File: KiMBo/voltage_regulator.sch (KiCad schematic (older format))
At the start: 13 parts

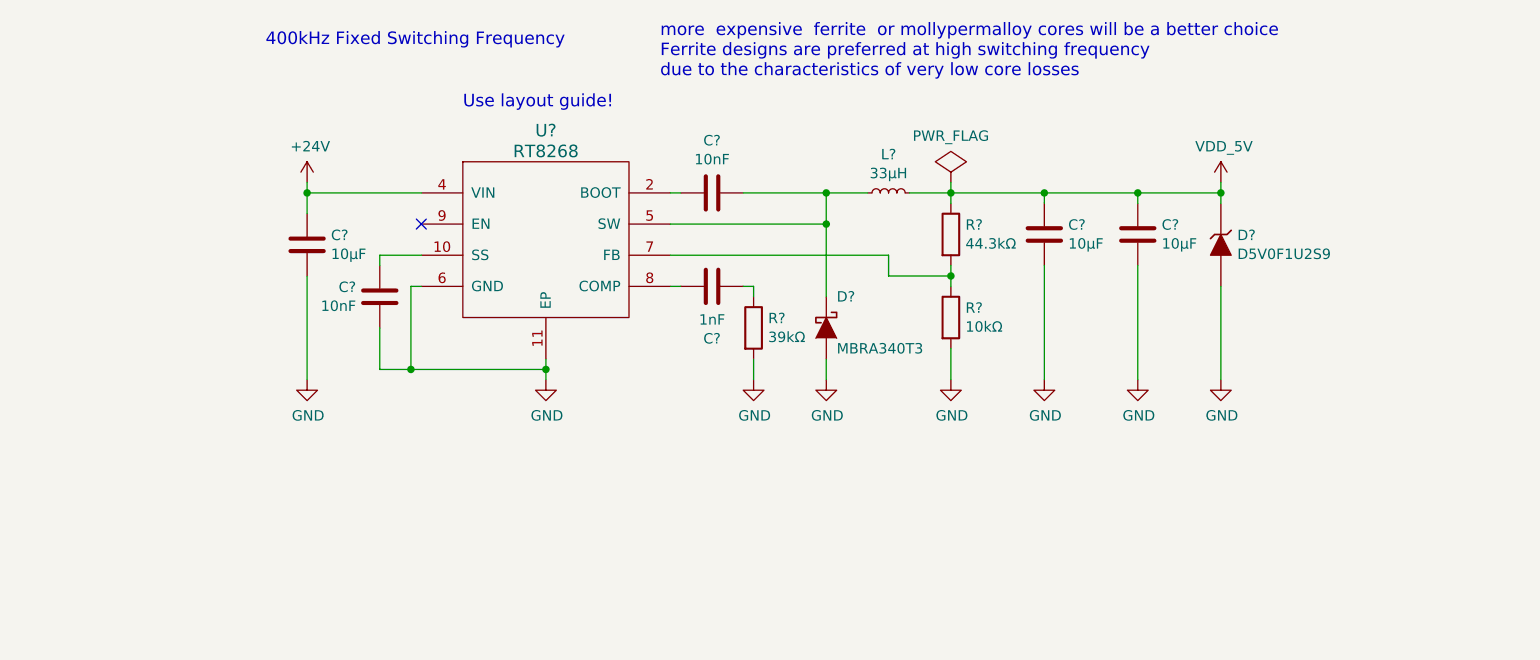
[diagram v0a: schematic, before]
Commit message: Move EN and SS lines, update 5V regulator passive values
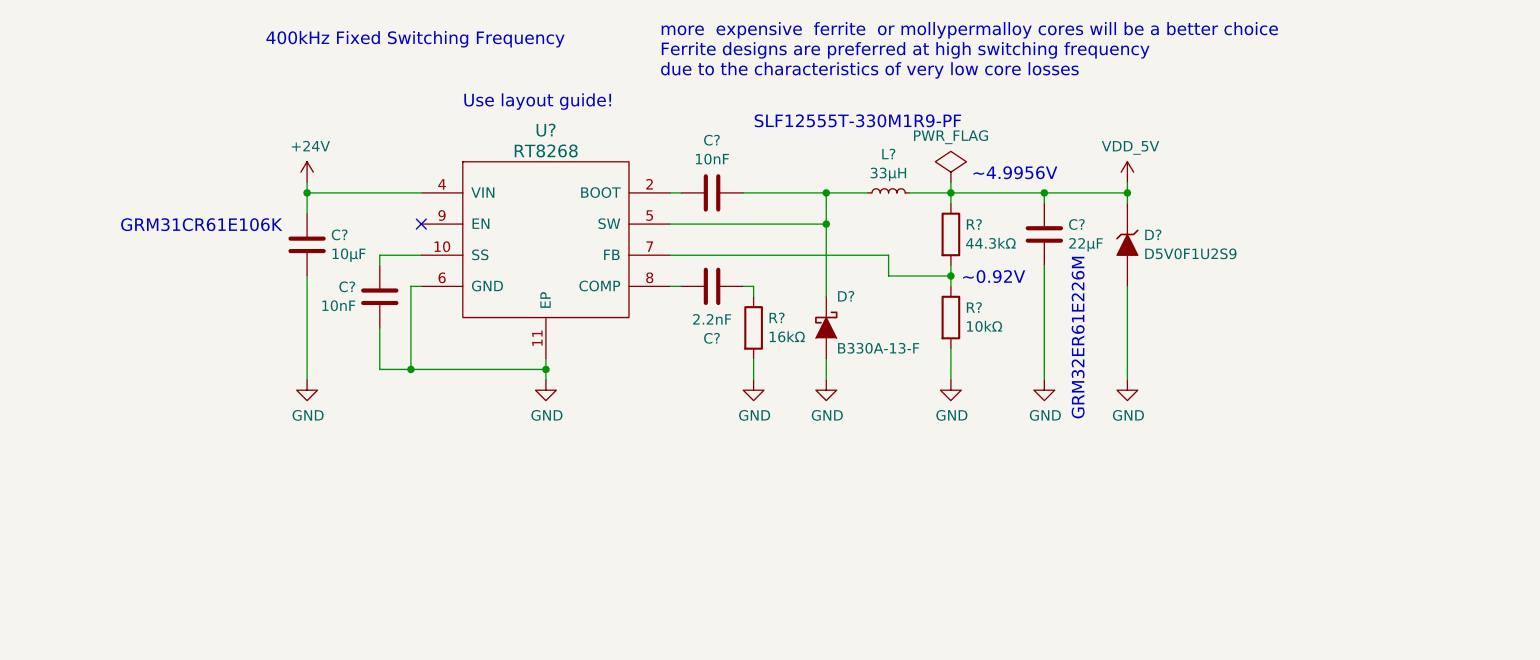
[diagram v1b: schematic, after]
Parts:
- removed C?: 10μF, symbol C
- C?: value 1nF -> 2.2nF
- C?: value 10μF -> 22μF
- D?: value MBRA340T3 -> B330A-13-F
- R?: value 39kΩ -> 16kΩ
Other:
- note added: "GRM31CR61E106K"
- note added: "GRM32ER61E226M"
- note added: "SLF12555T-330M1R9-PF"
- note added: "~~0.92V"
- note added: "~~4.9956V"
- moved on the sheet: D?
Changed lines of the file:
@@
 $EndDescr
 $Comp
-L PWR_FLAG #FLG053
+L PWR_FLAG #FLG074
 U 1 1 578901B0
 P 9250 4200
-F 0 "#FLG053" H 9250 4295 50  0001 C CNN
+F 0 "#FLG074" H 9250 4295 50  0001 C CNN
 F 1 "PWR_FLAG" H 9250 4424 50  0000 C CNN
 F 2 "" H 9250 4200 50  0000 C CNN
@@
 $EndComp
 $Comp
-L VDD_5V #PWR?
+L VDD_5V #PWR075
 U 1 1 59E9FFBE
-P 10550 4200
-F 0 "#PWR?" H 10550 4050 50  0001 C CNN
-F 1 "VDD_5V" H 10565 4373 50  0000 C CNN
-F 2 "" H 10550 4200 50  0000 C CNN
-F 3 "" H 10550 4200 50  0000 C CNN
-	1    10550 4200
+P 10100 4200
+F 0 "#PWR075" H 10100 4050 50  0001 C CNN
+F 1 "VDD_5V" H 10115 4373 50  0000 C CNN
+F 2 "" H 10100 4200 50  0000 C CNN
+F 3 "" H 10100 4200 50  0000 C CNN
+	1    10100 4200
 	1    0    0    -1
 $EndComp
@@
 	6700 4250 6150 4250
 $Comp
-L +24V #PWR?
+L +24V #PWR076
 U 1 1 59F3325A
 P 6150 4200
-F 0 "#PWR?" H 6150 4050 50  0001 C CNN
+F 0 "#PWR076" H 6150 4050 50  0001 C CNN
 F 1 "+24V" H 6165 4373 50  0000 C CNN
 F 2 "" H 6150 4200 50  0000 C CNN
@@
 $EndComp
 Wire Wire Line
-	6150 4200 6150 4350
+	6150 4200 6150 4250
+Wire Wire Line
+	6150 4250 6150 4350
 $Comp
 L C C?
@@
 	6650 4700 6650 5100
 Wire Wire Line
-	7300 5050 7300 5150
-$Comp
-L GND #PWR?
+	7300 5050 7300 5100
+Wire Wire Line
+	7300 5100 7300 5150
+$Comp
+L GND #PWR077
 U 1 1 59F333D1
 P 7300 5150
-F 0 "#PWR?" H 7300 4900 50  0001 C CNN
+F 0 "#PWR077" H 7300 4900 50  0001 C CNN
 F 1 "GND" H 7305 4977 50  0000 C CNN
 F 2 "" H 7300 5150 50  0000 C CNN
@@
 $EndComp
 Wire Wire Line
-	8250 4250 8850 4250
-Wire Wire Line
-	8650 4250 8650 4750
+	8250 4250 8650 4250
+Wire Wire Line
+	8650 4250 8850 4250
+Wire Wire Line
+	8650 4250 8650 4400
+Wire Wire Line
+	8650 4400 8650 4750
 Connection ~ 8650 4250
 $Comp
@@
 P 8100 4700
 F 0 "C?" V 8352 4700 50  0000 C CNN
-F 1 "1nF" V 8261 4700 50  0000 C CNN
+F 1 "2.2nF" V 8261 4700 50  0000 C CNN
 F 2 "" H 8138 4550 50  0000 C CNN
 F 3 "" H 8100 4700 50  0000 C CNN
@@
 P 8300 4900
 F 0 "R?" H 8370 4946 50  0000 L CNN
-F 1 "39kΩ" H 8370 4855 50  0000 L CNN
+F 1 "16kΩ" H 8370 4855 50  0000 L CNN
 F 2 "" V 8230 4900 50  0000 C CNN
 F 3 "" H 8300 4900 50  0000 C CNN
@@
 	7950 4700 7900 4700
 $Comp
-L GND #PWR?
+L GND #PWR078
 U 1 1 59F340C2
 P 8300 5150
-F 0 "#PWR?" H 8300 4900 50  0001 C CNN
+F 0 "#PWR078" H 8300 4900 50  0001 C CNN
 F 1 "GND" H 8305 4977 50  0000 C CNN
 F 2 "" H 8300 5150 50  0000 C CNN
@@
 $EndComp
 $Comp
-L GND #PWR?
+L GND #PWR079
 U 1 1 59F340EC
 P 8650 5150
-F 0 "#PWR?" H 8650 4900 50  0001 C CNN
+F 0 "#PWR079" H 8650 4900 50  0001 C CNN
 F 1 "GND" H 8655 4977 50  0000 C CNN
 F 2 "" H 8650 5150 50  0000 C CNN
@@
 $EndComp
 Wire Wire Line
-	9250 4200 9250 4300
+	9250 4200 9250 4250
+Wire Wire Line
+	9250 4250 9250 4300
 Connection ~ 9250 4250
 Wire Wire Line
-	9250 4600 9250 4700
+	9250 4600 9250 4650
+Wire Wire Line
+	9250 4650 9250 4700
 Connection ~ 9250 4650
 $Comp
@@
 P 9700 4450
 F 0 "C?" H 9815 4496 50  0000 L CNN
-F 1 "10μF" H 9815 4405 50  0000 L CNN
+F 1 "22μF" H 9815 4405 50  0000 L CNN
 F 2 "" H 9738 4300 50  0000 C CNN
 F 3 "" H 9700 4450 50  0000 C CNN
@@
 $EndComp
 $Comp
-L C C?
-U 1 1 59F34969
-P 10150 4450
-F 0 "C?" H 10265 4496 50  0000 L CNN
-F 1 "10μF" H 10265 4405 50  0000 L CNN
-F 2 "" H 10188 4300 50  0000 C CNN
-F 3 "" H 10150 4450 50  0000 C CNN
-	1    10150 4450
-	1    0    0    -1
-$EndComp
-$Comp
-L GND #PWR?
+L GND #PWR080
 U 1 1 59F34AA9
 P 9250 5150
-F 0 "#PWR?" H 9250 4900 50  0001 C CNN
+F 0 "#PWR080" H 9250 4900 50  0001 C CNN
 F 1 "GND" H 9255 4977 50  0000 C CNN
 F 2 "" H 9250 5150 50  0000 C CNN
@@
 Wire Wire Line
 	9700 4600 9700 5150
-Wire Wire Line
-	10150 4600 10150 5150
-$Comp
-L GND #PWR?
+$Comp
+L GND #PWR081
 U 1 1 59F34B40
 P 9700 5150
-F 0 "#PWR?" H 9700 4900 50  0001 C CNN
+F 0 "#PWR081" H 9700 4900 50  0001 C CNN
 F 1 "GND" H 9705 4977 50  0000 C CNN
 F 2 "" H 9700 5150 50  0000 C CNN
@@
 	1    0    0    -1
 $EndComp
-$Comp
-L GND #PWR?
-U 1 1 59F34B6F
-P 10150 5150
-F 0 "#PWR?" H 10150 4900 50  0001 C CNN
-F 1 "GND" H 10155 4977 50  0000 C CNN
-F 2 "" H 10150 5150 50  0000 C CNN
-F 3 "" H 10150 5150 50  0000 C CNN
-	1    10150 5150
-	1    0    0    -1
-$EndComp
 Wire Wire Line
 	9250 5000 9250 5150
@@
 NoConn ~ 6700 4400
 Wire Wire Line
-	6500 5100 7300 5100
-$Comp
-L GND #PWR?
+	6500 5100 6650 5100
+Wire Wire Line
+	6650 5100 7300 5100
+$Comp
+L GND #PWR083
 U 1 1 59F365D1
 P 6150 5150
-F 0 "#PWR?" H 6150 4900 50  0001 C CNN
+F 0 "#PWR083" H 6150 4900 50  0001 C CNN
 F 1 "GND" H 6155 4977 50  0000 C CNN
 F 2 "" H 6150 5150 50  0000 C CNN
@@
 L ZENER D?
 U 1 1 5B7841ED
-P 10550 4500
-F 0 "D?" V 10504 4579 50  0000 L CNN
-F 1 "D5V0F1U2S9" V 10595 4579 50  0000 L CNN
-F 2 "" H 10550 4500 50  0000 C CNN
-F 3 "" H 10550 4500 50  0000 C CNN
-	1    10550 4500
+P 10100 4500
+F 0 "D?" V 10054 4579 50  0000 L CNN
+F 1 "D5V0F1U2S9" V 10145 4579 50  0000 L CNN
+F 2 "" H 10100 4500 50  0000 C CNN
+F 3 "" H 10100 4500 50  0000 C CNN
+	1    10100 4500
 	0    1    1    0
 $EndComp
@@
 P 8650 4900
 F 0 "D?" V 8500 4950 50  0000 L CNN
-F 1 "MBRA340T3" V 8750 4950 50  0000 L CNN
+F 1 "B330A-13-F" V 8750 4950 50  0000 L CNN
 F 2 "" H 8650 4900 50  0000 C CNN
 F 3 "" H 8650 4900 50  0000 C CNN
@@
 $EndComp
 Wire Wire Line
-	10550 4200 10550 4300
-$Comp
-L GND #PWR?
+	10100 4200 10100 4250
+Wire Wire Line
+	10100 4250 10100 4300
+$Comp
+L GND #PWR084
 U 1 1 5B79111A
-P 10550 5150
-F 0 "#PWR?" H 10550 4900 50  0001 C CNN
-F 1 "GND" H 10555 4977 50  0000 C CNN
-F 2 "" H 10550 5150 50  0000 C CNN
-F 3 "" H 10550 5150 50  0000 C CNN
-	1    10550 5150
-	1    0    0    -1
-$EndComp
-Wire Wire Line
-	10550 5150 10550 4700
-Wire Wire Line
-	9050 4250 10550 4250
-Wire Wire Line
-	10150 4250 10150 4300
-Connection ~ 10150 4250
-Connection ~ 10550 4250
+P 10100 5150
+F 0 "#PWR084" H 10100 4900 50  0001 C CNN
+F 1 "GND" H 10105 4977 50  0000 C CNN
+F 2 "" H 10100 5150 50  0000 C CNN
+F 3 "" H 10100 5150 50  0000 C CNN
+	1    10100 5150
+	1    0    0    -1
+$EndComp
+Wire Wire Line
+	10100 5150 10100 4700
+Connection ~ 10100 4250
+Text Notes 9300 4700 0    60   ~ 0
+~~0.92V
+Text Notes 9350 4200 0    60   ~ 0
+~~4.9956V
+Wire Wire Line
+	9050 4250 9250 4250
+Wire Wire Line
+	9250 4250 9700 4250
+Wire Wire Line
+	9700 4250 10100 4250
+Text Notes 9900 5350 1    60   ~ 0
+GRM32ER61E226M
+Text Notes 8300 3950 0    60   ~ 0
+SLF12555T-330M1R9-PF
+Text Notes 5250 4450 0    60   ~ 0
+GRM31CR61E106K
 $EndSCHEMATC

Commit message: Annotate all components, now passing ERC, added ferrites to the rest of the connectors
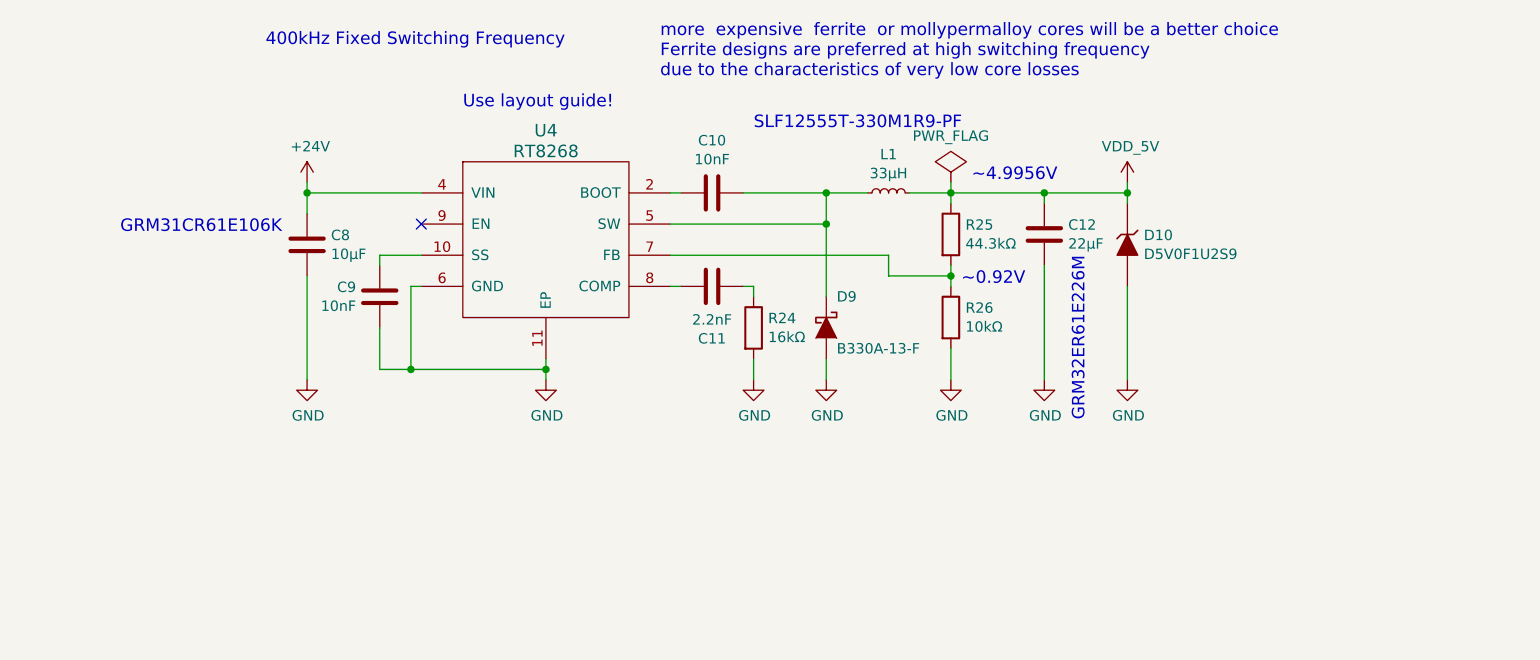
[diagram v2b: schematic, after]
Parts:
- gave numbers to parts that had none: 12
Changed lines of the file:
@@
 $EndComp
 $Comp
-L RT8268 U?
+L RT8268 U4
 U 1 1 59F30B79
 P 7300 4500
-F 0 "U?" H 7300 5050 60  0000 C CNN
+F 0 "U4" H 7300 5050 60  0000 C CNN
 F 1 "RT8268" H 7300 4950 60  0000 C CNN
 F 2 "" H 7300 4500 60  0000 C CNN
@@
 $EndComp
 $Comp
-L C C?
+L C C8
 U 1 1 59F33160
 P 6150 4500
-F 0 "C?" H 6265 4546 50  0000 L CNN
+F 0 "C8" H 6265 4546 50  0000 L CNN
 F 1 "10μF" H 6265 4455 50  0000 L CNN
 F 2 "" H 6188 4350 50  0000 C CNN
@@
 $EndComp
 Wire Wire Line
-	6150 4200 6150 4250
-Wire Wire Line
-	6150 4250 6150 4350
-$Comp
-L C C?
+	6150 4200 6150 4350
+$Comp
+L C C9
 U 1 1 59F33331
 P 6500 4750
-F 0 "C?" H 6614 4796 50  0000 L CNN
+F 0 "C9" H 6614 4796 50  0000 L CNN
 F 1 "10nF" H 6614 4705 50  0000 L CNN
 F 2 "" H 6538 4600 50  0000 C CNN
@@
 	6650 4700 6650 5100
 Wire Wire Line
-	7300 5050 7300 5100
-Wire Wire Line
-	7300 5100 7300 5150
+	7300 5050 7300 5150
 $Comp
 L GND #PWR077
@@
 Connection ~ 6150 4250
 $Comp
-L C C?
+L C C10
 U 1 1 59F33CB6
 P 8100 4250
-F 0 "C?" V 7848 4250 50  0000 C CNN
+F 0 "C10" V 7848 4250 50  0000 C CNN
 F 1 "10nF" V 7939 4250 50  0000 C CNN
 F 2 "" H 8138 4100 50  0000 C CNN
@@
 	7950 4250 7900 4250
 $Comp
-L INDUCTOR_Small L?
+L INDUCTOR_Small L1
 U 1 1 59F33EC0
 P 8950 4250
-F 0 "L?" V 9135 4250 50  0000 C CNN
+F 0 "L1" V 9135 4250 50  0000 C CNN
 F 1 "33μH" V 9044 4250 50  0000 C CNN
 F 2 "" H 8950 4250 50  0000 C CNN
@@
 $EndComp
 Wire Wire Line
-	8250 4250 8650 4250
-Wire Wire Line
-	8650 4250 8850 4250
-Wire Wire Line
-	8650 4250 8650 4400
-Wire Wire Line
-	8650 4400 8650 4750
+	8250 4250 8850 4250
+Wire Wire Line
+	8650 4250 8650 4750
 Connection ~ 8650 4250
 $Comp
-L C C?
+L C C11
 U 1 1 59F33F7A
 P 8100 4700
-F 0 "C?" V 8352 4700 50  0000 C CNN
+F 0 "C11" V 8352 4700 50  0000 C CNN
 F 1 "2.2nF" V 8261 4700 50  0000 C CNN
 F 2 "" H 8138 4550 50  0000 C CNN
@@
 $EndComp
 $Comp
-L R R?
+L R R24
 U 1 1 59F33FE9
 P 8300 4900
-F 0 "R?" H 8370 4946 50  0000 L CNN
+F 0 "R24" H 8370 4946 50  0000 L CNN
 F 1 "16kΩ" H 8370 4855 50  0000 L CNN
 F 2 "" V 8230 4900 50  0000 C CNN
@@
 	8300 5150 8300 5050
 $Comp
-L R R?
+L R R25
 U 1 1 59F344C0
 P 9250 4450
-F 0 "R?" H 9320 4496 50  0000 L CNN
+F 0 "R25" H 9320 4496 50  0000 L CNN
 F 1 "44.3kΩ" H 9320 4405 50  0000 L CNN
 F 2 "" V 9180 4450 50  0000 C CNN
@@
 $EndComp
 $Comp
-L R R?
+L R R26
 U 1 1 59F344FF
 P 9250 4850
-F 0 "R?" H 9320 4896 50  0000 L CNN
+F 0 "R26" H 9320 4896 50  0000 L CNN
 F 1 "10kΩ" H 9320 4805 50  0000 L CNN
 F 2 "" V 9180 4850 50  0000 C CNN
@@
 $EndComp
 Wire Wire Line
-	9250 4200 9250 4250
-Wire Wire Line
-	9250 4250 9250 4300
+	9250 4200 9250 4300
 Connection ~ 9250 4250
 Wire Wire Line
-	9250 4600 9250 4650
-Wire Wire Line
-	9250 4650 9250 4700
+	9250 4600 9250 4700
 Connection ~ 9250 4650
 $Comp
-L C C?
+L C C12
 U 1 1 59F34902
 P 9700 4450
-F 0 "C?" H 9815 4496 50  0000 L CNN
+F 0 "C12" H 9815 4496 50  0000 L CNN
 F 1 "22μF" H 9815 4405 50  0000 L CNN
 F 2 "" H 9738 4300 50  0000 C CNN
@@
 	9250 5000 9250 5150
 Wire Wire Line
-	9700 4300 9700 4250
+	9700 4250 9700 4300
 Connection ~ 9700 4250
 Wire Wire Line
@@
 NoConn ~ 6700 4400
 Wire Wire Line
-	6500 5100 6650 5100
-Wire Wire Line
-	6650 5100 7300 5100
-$Comp
-L GND #PWR083
+	6500 5100 7300 5100
+$Comp
+L GND #PWR082
 U 1 1 59F365D1
 P 6150 5150
-F 0 "#PWR083" H 6150 4900 50  0001 C CNN
+F 0 "#PWR082" H 6150 4900 50  0001 C CNN
 F 1 "GND" H 6155 4977 50  0000 C CNN
 F 2 "" H 6150 5150 50  0000 C CNN
@@
 	8950 4650 9250 4650
 $Comp
-L ZENER D?
+L ZENER D10
 U 1 1 5B7841ED
 P 10100 4500
-F 0 "D?" V 10054 4579 50  0000 L CNN
+F 0 "D10" V 10054 4579 50  0000 L CNN
 F 1 "D5V0F1U2S9" V 10145 4579 50  0000 L CNN
 F 2 "" H 10100 4500 50  0000 C CNN
@@
 $EndComp
 $Comp
-L D_Schottky D?
+L D_Schottky D9
 U 1 1 5B78FD55
 P 8650 4900
-F 0 "D?" V 8500 4950 50  0000 L CNN
+F 0 "D9" V 8500 4950 50  0000 L CNN
 F 1 "B330A-13-F" V 8750 4950 50  0000 L CNN
 F 2 "" H 8650 4900 50  0000 C CNN
@@
 $EndComp
 Wire Wire Line
-	10100 4200 10100 4250
-Wire Wire Line
-	10100 4250 10100 4300
-$Comp
-L GND #PWR084
+	10100 4200 10100 4300
+$Comp
+L GND #PWR083
 U 1 1 5B79111A
 P 10100 5150
-F 0 "#PWR084" H 10100 4900 50  0001 C CNN
+F 0 "#PWR083" H 10100 4900 50  0001 C CNN
 F 1 "GND" H 10105 4977 50  0000 C CNN
 F 2 "" H 10100 5150 50  0000 C CNN
@@
 ~~4.9956V
 Wire Wire Line
-	9050 4250 9250 4250
-Wire Wire Line
-	9250 4250 9700 4250
-Wire Wire Line
-	9700 4250 10100 4250
+	9050 4250 10100 4250
 Text Notes 9900 5350 1    60   ~ 0
 GRM32ER61E226M

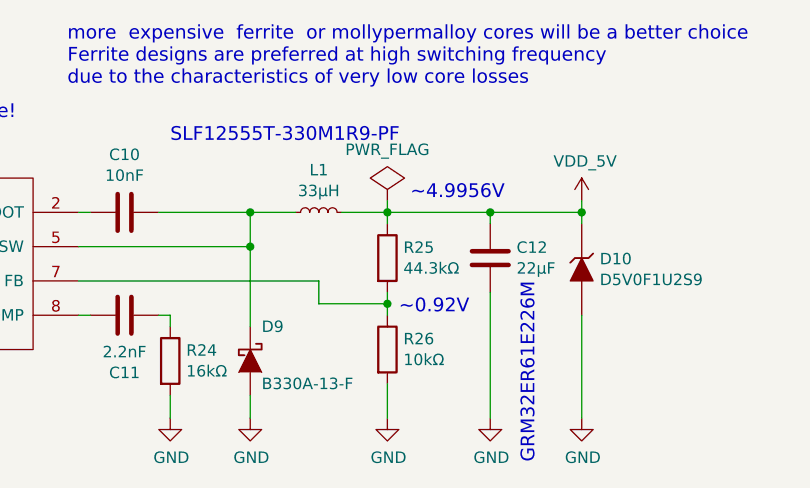
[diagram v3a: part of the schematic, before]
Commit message: Entry of additional component values
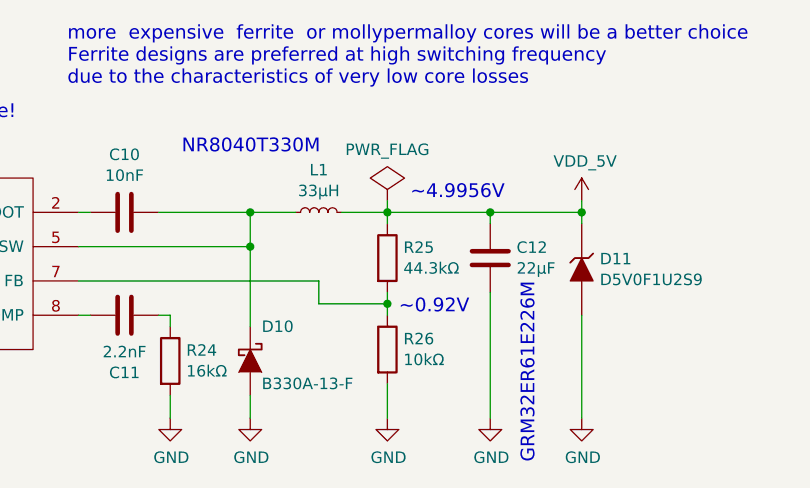
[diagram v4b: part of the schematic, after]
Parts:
- renumbered D9 to D10, D10 to D11
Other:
- note added: "NR8040T330M"
- note removed: "SLF12555T-330M1R9-PF"
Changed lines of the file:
@@
 $EndDescr
 $Comp
-L PWR_FLAG #FLG074
+L PWR_FLAG #FLG075
 U 1 1 578901B0
 P 9250 4200
-F 0 "#FLG074" H 9250 4295 50  0001 C CNN
+F 0 "#FLG075" H 9250 4295 50  0001 C CNN
 F 1 "PWR_FLAG" H 9250 4424 50  0000 C CNN
 F 2 "" H 9250 4200 50  0000 C CNN
@@
 $EndComp
 $Comp
-L VDD_5V #PWR075
+L VDD_5V #PWR076
 U 1 1 59E9FFBE
 P 10100 4200
-F 0 "#PWR075" H 10100 4050 50  0001 C CNN
+F 0 "#PWR076" H 10100 4050 50  0001 C CNN
 F 1 "VDD_5V" H 10115 4373 50  0000 C CNN
 F 2 "" H 10100 4200 50  0000 C CNN
@@
 	6700 4250 6150 4250
 $Comp
-L +24V #PWR076
+L +24V #PWR077
 U 1 1 59F3325A
 P 6150 4200
-F 0 "#PWR076" H 6150 4050 50  0001 C CNN
+F 0 "#PWR077" H 6150 4050 50  0001 C CNN
 F 1 "+24V" H 6165 4373 50  0000 C CNN
 F 2 "" H 6150 4200 50  0000 C CNN
@@
 	7300 5050 7300 5150
 $Comp
-L GND #PWR077
+L GND #PWR078
 U 1 1 59F333D1
 P 7300 5150
-F 0 "#PWR077" H 7300 4900 50  0001 C CNN
+F 0 "#PWR078" H 7300 4900 50  0001 C CNN
 F 1 "GND" H 7305 4977 50  0000 C CNN
 F 2 "" H 7300 5150 50  0000 C CNN
@@
 	7950 4700 7900 4700
 $Comp
-L GND #PWR078
+L GND #PWR079
 U 1 1 59F340C2
 P 8300 5150
-F 0 "#PWR078" H 8300 4900 50  0001 C CNN
+F 0 "#PWR079" H 8300 4900 50  0001 C CNN
 F 1 "GND" H 8305 4977 50  0000 C CNN
 F 2 "" H 8300 5150 50  0000 C CNN
@@
 $EndComp
 $Comp
-L GND #PWR079
+L GND #PWR080
 U 1 1 59F340EC
 P 8650 5150
-F 0 "#PWR079" H 8650 4900 50  0001 C CNN
+F 0 "#PWR080" H 8650 4900 50  0001 C CNN
 F 1 "GND" H 8655 4977 50  0000 C CNN
 F 2 "" H 8650 5150 50  0000 C CNN
@@
 $EndComp
 $Comp
-L GND #PWR080
+L GND #PWR081
 U 1 1 59F34AA9
 P 9250 5150
-F 0 "#PWR080" H 9250 4900 50  0001 C CNN
+F 0 "#PWR081" H 9250 4900 50  0001 C CNN
 F 1 "GND" H 9255 4977 50  0000 C CNN
 F 2 "" H 9250 5150 50  0000 C CNN
@@
 	9700 4600 9700 5150
 $Comp
-L GND #PWR081
+L GND #PWR082
 U 1 1 59F34B40
 P 9700 5150
-F 0 "#PWR081" H 9700 4900 50  0001 C CNN
+F 0 "#PWR082" H 9700 4900 50  0001 C CNN
 F 1 "GND" H 9705 4977 50  0000 C CNN
 F 2 "" H 9700 5150 50  0000 C CNN
@@
 	6500 5100 7300 5100
 $Comp
-L GND #PWR082
+L GND #PWR083
 U 1 1 59F365D1
 P 6150 5150
-F 0 "#PWR082" H 6150 4900 50  0001 C CNN
+F 0 "#PWR083" H 6150 4900 50  0001 C CNN
 F 1 "GND" H 6155 4977 50  0000 C CNN
 F 2 "" H 6150 5150 50  0000 C CNN
@@
 	8950 4650 9250 4650
 $Comp
-L ZENER D10
+L ZENER D11
 U 1 1 5B7841ED
 P 10100 4500
-F 0 "D10" V 10054 4579 50  0000 L CNN
+F 0 "D11" V 10054 4579 50  0000 L CNN
 F 1 "D5V0F1U2S9" V 10145 4579 50  0000 L CNN
 F 2 "" H 10100 4500 50  0001 C CNN
@@
 $EndComp
 $Comp
-L D_Schottky D9
+L D_Schottky D10
 U 1 1 5B78FD55
 P 8650 4900
-F 0 "D9" V 8500 4950 50  0000 L CNN
+F 0 "D10" V 8500 4950 50  0000 L CNN
 F 1 "B330A-13-F" V 8750 4950 50  0000 L CNN
 F 2 "" H 8650 4900 50  0001 C CNN
@@
 	10100 4200 10100 4300
 $Comp
-L GND #PWR083
+L GND #PWR084
 U 1 1 5B79111A
 P 10100 5150
-F 0 "#PWR083" H 10100 4900 50  0001 C CNN
+F 0 "#PWR084" H 10100 4900 50  0001 C CNN
 F 1 "GND" H 10105 4977 50  0000 C CNN
 F 2 "" H 10100 5150 50  0000 C CNN
@@
 Text Notes 9900 5350 1    60   ~ 0
 GRM32ER61E226M
-Text Notes 8300 3950 0    60   ~ 0
-SLF12555T-330M1R9-PF
+Text Notes 8350 4000 0    60   ~ 0
+NR8040T330M
 Text Notes 5250 4450 0    60   ~ 0
 GRM31CR61E106K
